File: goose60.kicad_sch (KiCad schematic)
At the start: 1 part

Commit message: add new design
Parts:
- added C1, C2: 22pF, symbol Device:C_Small
- added C3: 1uF, symbol Device:C_Small
- added C4, C5, C6, C7: 100nF, symbol Device:C_Small
- added D1, D2, D3: LED, symbol Device:LED
- added R1, R2: 10K, Resistor_SMD:R_0805_2012Metric, symbol Device:R_Small
- added R3: 300, symbol Device:R_Small
- added SW1, SW2: SW_Push, Button_Switch_SMD:SW_Push_1P1T_NO_CK_KSC6xxJ, symbol Switch:SW_Push
- added X1: Crystal_GND24, symbol Device:Crystal_GND24
- gave numbers to parts that had none: 1
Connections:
- net +3.3V: now reaches U1.1 (VBAT)
- net +3.3V: now also U1.24 (VDD), U1.36 (VDD), U1.48 (VDD), U1.9 (VDDA), C3.1, C4.1, C5.1, C6.1, C7.1, D1.2 (A), D2.2 (A), D3.2 (A), R1.1, R2.1
- net row5: now reaches U1.11 (PA1)
- net row4: now reaches U1.12 (PA2)
- net row3: now reaches U1.13 (PA3)
- net CAPS_LED: now reaches U1.14 (PA4)
- net CAPS_LED: now also R3.2
- net SCK: now reaches U1.15 (PA5)
- net MISO: now reaches U1.16 (PA6)
- net MOSI: now reaches U1.17 (PA7)
- net row2: now reaches U1.18 (PB0)
- net row1: now reaches U1.19 (PB1)
- net col8: now reaches U1.20 (PB2)
- net col9: now reaches U1.21 (PB10)
- net col10: now reaches U1.22 (PB11)
- net GND: now reaches U1.23 (VSS)
- net GND: now also U1.35 (VSS), U1.47 (VSS), U1.8 (VSSA), C1.2, C2.2, C3.2, C4.2, C5.2, C6.2, C7.2, SW1.1, SW2.1, X1.2, X1.4
- net col11: now reaches U1.25 (PB12)
- net col12: now reaches U1.26 (PB13)
- net col13: now reaches U1.27 (PB14)
- net col14: now reaches U1.28 (PB15)
- net MCU_TX: now reaches U1.30 (PA9)
- net MCU_RX: now reaches U1.31 (PA10)
- net USB_D-: now reaches U1.32 (PA11)
- net USB_D+: now reaches U1.33 (PA12)
- net SWDIO: now reaches U1.34 (PA13)
- net SWCLK: now reaches U1.37 (PA14)
- net col1: now reaches U1.39 (PB3)
- net col2: now reaches U1.40 (PB4)
- net col3: now reaches U1.41 (PB5)
- net col4: now reaches U1.42 (PB6)
- net col5: now reaches U1.43 (PB7)
- net BOOT0: now reaches U1.44 (BOOT0)
- net BOOT0: now also R1.2, SW1.2
- net col6: now reaches U1.45 (PB8)
- net col7: now reaches U1.46 (PB9)
- net XTAL1: now reaches U1.5 (PD0)
- net XTAL1: now also C1.1, X1.1
- net XTAL2: now reaches U1.6 (PD1)
- net XTAL2: now also C2.1, X1.3
- net RESET: now reaches U1.7 (NRST)
- net RESET: now also R2.2, SW2.2
- new net: D1.1 (K), D2.1 (K), D3.1 (K), R3.1
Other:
- added sheet Interface (Interface.kicad_sch)
- added sheet PowerManager (PowerManager.kicad_sch)
- added sheet keyswitches (switches.kicad_sch)
- moved on the sheet: U1

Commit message: update goose60 sch footprint
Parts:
- C1, C2, C3, C4, C5, C6, C7: footprint (none) -> Capacitor_SMD:C_0201_0603Metric
- D1, D2, D3: footprint (none) -> LED_SMD:LED_0805_2012Metric
- R3: footprint (none) -> Resistor_SMD:R_0805_2012Metric
- X1: footprint (none) -> Crystal:Crystal_SMD_TXC_7M-4Pin_3.2x2.5mm

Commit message: update components location
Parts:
- C1, C2, C3, C4, C5, C6, C7: footprint Capacitor_SMD:C_0201_0603Metric -> Capacitor_SMD:C_0603_1608Metric
- R1, R2, R3: footprint Resistor_SMD:R_0805_2012Metric -> Resistor_SMD:R_0603_1608Metric
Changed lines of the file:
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@@
       (effects (font (size 1.27 1.27)) (justify left))
     )
-    (property "Footprint" "Capacitor_SMD:C_0201_0603Metric" (id 2) (at 113.03 44.45 0)
+    (property "Footprint" "Capacitor_SMD:C_0603_1608Metric" (id 2) (at 113.03 44.45 0)
       (effects (font (size 1.27 1.27)) hide)
     )
@@
       (effects (font (size 1.27 1.27)) (justify left))
     )
-    (property "Footprint" "Resistor_SMD:R_0805_2012Metric" (id 2) (at 30.48 38.1 0)
+    (property "Footprint" "Resistor_SMD:R_0603_1608Metric" (id 2) (at 30.48 38.1 0)
       (effects (font (size 1.27 1.27)) hide)
     )
@@
       (effects (font (size 1.27 1.27)) (justify left))
     )
-    (property "Footprint" "Capacitor_SMD:C_0201_0603Metric" (id 2) (at 90.17 44.45 0)
+    (property "Footprint" "Capacitor_SMD:C_0603_1608Metric" (id 2) (at 90.17 44.45 0)
       (effects (font (size 1.27 1.27)) hide)
     )
@@
       (effects (font (size 1.27 1.27)) (justify left))
     )
-    (property "Footprint" "Capacitor_SMD:C_0201_0603Metric" (id 2) (at 101.6 44.45 0)
+    (property "Footprint" "Capacitor_SMD:C_0603_1608Metric" (id 2) (at 101.6 44.45 0)
       (effects (font (size 1.27 1.27)) hide)
     )
@@
     (property "Reference" "R3" (id 0) (at 248.92 153.67 90))
     (property "Value" "300" (id 1) (at 248.92 151.13 90))
-    (property "Footprint" "Resistor_SMD:R_0805_2012Metric" (id 2) (at 248.92 148.59 0)
+    (property "Footprint" "Resistor_SMD:R_0603_1608Metric" (id 2) (at 248.92 148.59 0)
       (effects (font (size 1.27 1.27)) hide)
     )
@@
       (effects (font (size 1.27 1.27)) (justify left))
     )
-    (property "Footprint" "Resistor_SMD:R_0805_2012Metric" (id 2) (at 55.88 38.1 0)
+    (property "Footprint" "Resistor_SMD:R_0603_1608Metric" (id 2) (at 55.88 38.1 0)
       (effects (font (size 1.27 1.27)) hide)
     )
@@
       (effects (font (size 1.27 1.27)) (justify left))
     )
-    (property "Footprint" "Capacitor_SMD:C_0201_0603Metric" (id 2) (at 52.07 91.44 0)
+    (property "Footprint" "Capacitor_SMD:C_0603_1608Metric" (id 2) (at 52.07 91.44 0)
       (effects (font (size 1.27 1.27)) hide)
     )
@@
       (effects (font (size 1.27 1.27)) (justify left))
     )
-    (property "Footprint" "Capacitor_SMD:C_0201_0603Metric" (id 2) (at 124.46 44.45 0)
+    (property "Footprint" "Capacitor_SMD:C_0603_1608Metric" (id 2) (at 124.46 44.45 0)
       (effects (font (size 1.27 1.27)) hide)
     )
@@
       (effects (font (size 1.27 1.27)) (justify left))
     )
-    (property "Footprint" "Capacitor_SMD:C_0201_0603Metric" (id 2) (at 80.01 44.45 0)
+    (property "Footprint" "Capacitor_SMD:C_0603_1608Metric" (id 2) (at 80.01 44.45 0)
       (effects (font (size 1.27 1.27)) hide)
     )
@@
       (effects (font (size 1.27 1.27)) (justify left))
     )
-    (property "Footprint" "Capacitor_SMD:C_0201_0603Metric" (id 2) (at 34.29 91.44 0)
+    (property "Footprint" "Capacitor_SMD:C_0603_1608Metric" (id 2) (at 34.29 91.44 0)
       (effects (font (size 1.27 1.27)) hide)
     )
@@
     )
     (path "/f9fe2ed8-a3e3-4d28-b983-2bb5b9d6e010"
-      (reference "C1") (unit 1) (value "22pF") (footprint "Capacitor_SMD:C_0201_0603Metric")
+      (reference "C1") (unit 1) (value "22pF") (footprint "Capacitor_SMD:C_0603_1608Metric")
     )
     (path "/85b1023e-0f04-495c-899c-b4db4874d87f"
-      (reference "C2") (unit 1) (value "22pF") (footprint "Capacitor_SMD:C_0201_0603Metric")
+      (reference "C2") (unit 1) (value "22pF") (footprint "Capacitor_SMD:C_0603_1608Metric")
     )
     (path "/a3141805-9795-46b8-a319-4a53200c12ca"
-      (reference "C3") (unit 1) (value "1uF") (footprint "Capacitor_SMD:C_0201_0603Metric")
+      (reference "C3") (unit 1) (value "1uF") (footprint "Capacitor_SMD:C_0603_1608Metric")
     )
     (path "/5591f67d-166e-4c19-99b1-3b158056aa2d"
-      (reference "C4") (unit 1) (value "100nF") (footprint "Capacitor_SMD:C_0201_0603Metric")
+      (reference "C4") (unit 1) (value "100nF") (footprint "Capacitor_SMD:C_0603_1608Metric")
     )
     (path "/693c6004-a004-4312-bba3-757057e9f797"
-      (reference "C5") (unit 1) (value "100nF") (footprint "Capacitor_SMD:C_0201_0603Metric")
+      (reference "C5") (unit 1) (value "100nF") (footprint "Capacitor_SMD:C_0603_1608Metric")
     )
     (path "/17abe64e-64c1-4764-943d-a43538caeb21"
-      (reference "C6") (unit 1) (value "100nF") (footprint "Capacitor_SMD:C_0201_0603Metric")
+      (reference "C6") (unit 1) (value "100nF") (footprint "Capacitor_SMD:C_0603_1608Metric")
     )
     (path "/88d48de7-d7dd-45f7-8cfd-77da8f4dadfe"
-      (reference "C7") (unit 1) (value "100nF") (footprint "Capacitor_SMD:C_0201_0603Metric")
+      (reference "C7") (unit 1) (value "100nF") (footprint "Capacitor_SMD:C_0603_1608Metric")
     )
     (path "/01ad3d1c-4e51-419d-9147-129ed3c97a58/59366270-d046-4a8d-8a86-fa3f9d2a71fc"
-      (reference "C8") (unit 1) (value "100nF/16v") (footprint "Capacitor_SMD:C_0201_0603Metric")
+      (reference "C8") (unit 1) (value "100nF/16v") (footprint "Capacitor_SMD:C_0603_1608Metric")
     )
     (path "/01ad3d1c-4e51-419d-9147-129ed3c97a58/f33d1f7b-69f3-44d0-8d3e-63e68406121a"
-      (reference "C9") (unit 1) (value "10uF/16v") (footprint "Capacitor_SMD:C_0201_0603Metric")
+      (reference "C9") (unit 1) (value "10uF/16v") (footprint "Capacitor_SMD:C_0603_1608Metric")
     )
     (path "/01ad3d1c-4e51-419d-9147-129ed3c97a58/c9bdc69b-046c-48e6-81b1-bae8188675f3"
-      (reference "C10") (unit 1) (value "100uF/16v") (footprint "Capacitor_SMD:C_0201_0603Metric")
+      (reference "C10") (unit 1) (value "100uF/16v") (footprint "Capacitor_SMD:C_0603_1608Metric")
     )
     (path "/01ad3d1c-4e51-419d-9147-129ed3c97a58/6bfc3026-825b-4595-81dc-f862b2691dba"
-      (reference "C11") (unit 1) (value "100nF/16v") (footprint "Capacitor_SMD:C_0201_0603Metric")
+      (reference "C11") (unit 1) (value "100nF/16v") (footprint "Capacitor_SMD:C_0603_1608Metric")
     )
     (path "/a91e1d94-3d93-4a93-b820-1f6e8519d9a9"
@@
     )
     (path "/01ad3d1c-4e51-419d-9147-129ed3c97a58/5ebc741d-6cfd-4dfe-84d0-b07ee0e888cf"
-      (reference "D69") (unit 1) (value "6.3V/100V") (footprint "Diode_SMD:D_SOD-323F")
+      (reference "D69") (unit 1) (value "6.3V/100V") (footprint "Diode_SMD:D_0603_1608Metric")
     )
     (path "/01ad3d1c-4e51-419d-9147-129ed3c97a58/e45f4eff-fcf1-42db-a4e4-d19097900666"
-      (reference "D70") (unit 1) (value "1SS355TE") (footprint "Diode_SMD:D_SOD-323F")
+      (reference "D70") (unit 1) (value "1SS355TE") (footprint "Diode_SMD:D_0603_1608Metric")
     )
     (path "/62b6fb8f-6304-48f3-b35d-3d0f8813eb4a/693deba9-5b7b-47eb-a076-785918ecb9b5"
@@
     )
     (path "/24d5275e-ddc5-47af-b388-ecc08567cc69"
-      (reference "R1") (unit 1) (value "10K") (footprint "Resistor_SMD:R_0805_2012Metric")
+      (reference "R1") (unit 1) (value "10K") (footprint "Resistor_SMD:R_0603_1608Metric")
     )
     (path "/80049181-0e53-46a8-92f2-82ffb9ac51b9"
-      (reference "R2") (unit 1) (value "10K") (footprint "Resistor_SMD:R_0805_2012Metric")
+      (reference "R2") (unit 1) (value "10K") (footprint "Resistor_SMD:R_0603_1608Metric")
     )
     (path "/6a760a19-5869-4605-bfdf-467b2efd2302"
-      (reference "R3") (unit 1) (value "300") (footprint "Resistor_SMD:R_0805_2012Metric")
+      (reference "R3") (unit 1) (value "300") (footprint "Resistor_SMD:R_0603_1608Metric")
     )
     (path "/01ad3d1c-4e51-419d-9147-129ed3c97a58/58c52a8a-44f3-4097-86b6-0bb03693e54a"
-      (reference "R4") (unit 1) (value "240R/5%") (footprint "Resistor_SMD:R_0805_2012Metric")
+      (reference "R4") (unit 1) (value "240R/5%") (footprint "Resistor_SMD:R_0603_1608Metric")
     )
     (path "/01ad3d1c-4e51-419d-9147-129ed3c97a58/ffd8a55c-ebe3-49d3-8e38-b48450d53cd0"
-      (reference "R5") (unit 1) (value "820R/5%") (footprint "Resistor_SMD:R_0805_2012Metric")
+      (reference "R5") (unit 1) (value "820R/5%") (footprint "Resistor_SMD:R_0603_1608Metric")
     )
     (path "/01ad3d1c-4e51-419d-9147-129ed3c97a58/8fc35c16-fc9a-4e74-93e4-98f97ca6399b"
-      (reference "R6") (unit 1) (value "820R/5%") (footprint "Resistor_SMD:R_0805_2012Metric")
+      (reference "R6") (unit 1) (value "820R/5%") (footprint "Resistor_SMD:R_0603_1608Metric")
     )
     (path "/62b6fb8f-6304-48f3-b35d-3d0f8813eb4a/916bb521-d79a-4258-8831-772571d1f9b5"
-      (reference "R7") (unit 1) (value "10K") (footprint "Resistor_SMD:R_0805_2012Metric")
+      (reference "R7") (unit 1) (value "10K") (footprint "Resistor_SMD:R_0603_1608Metric")
     )
     (path "/62b6fb8f-6304-48f3-b35d-3d0f8813eb4a/052e406a-cd5c-4294-8787-61de419cd69b"
-      (reference "R8") (unit 1) (value "10K") (footprint "Resistor_SMD:R_0805_2012Metric")
+      (reference "R8") (unit 1) (value "10K") (footprint "Resistor_SMD:R_0603_1608Metric")
     )
     (path "/62b6fb8f-6304-48f3-b35d-3d0f8813eb4a/baffa815-068c-492b-b76f-cfe58c1daf53"
@@
     )
     (path "/62b6fb8f-6304-48f3-b35d-3d0f8813eb4a/75fd90a4-2c53-46a9-93a4-07f79f00b17a"
-      (reference "R12") (unit 1) (value "0") (footprint "Resistor_SMD:R_0805_2012Metric")
+      (reference "R12") (unit 1) (value "0") (footprint "Resistor_SMD:R_0603_1608Metric")
     )
     (path "/62b6fb8f-6304-48f3-b35d-3d0f8813eb4a/bbf19c51-7502-4c71-bd92-745e7b08f5a5"
-      (reference "R13") (unit 1) (value "0") (footprint "Resistor_SMD:R_0805_2012Metric")
+      (reference "R13") (unit 1) (value "0") (footprint "Resistor_SMD:R_0603_1608Metric")
     )
     (path "/62b6fb8f-6304-48f3-b35d-3d0f8813eb4a/3a4d123e-3d6c-458b-8cdb-27ddea7e40e5"
-      (reference "R14") (unit 1) (value "0") (footprint "Resistor_SMD:R_0805_2012Metric")
+      (reference "R14") (unit 1) (value "0") (footprint "Resistor_SMD:R_0603_1608Metric")
     )
     (path "/4b620212-7d38-40bd-8ffb-1e64542d8c37"

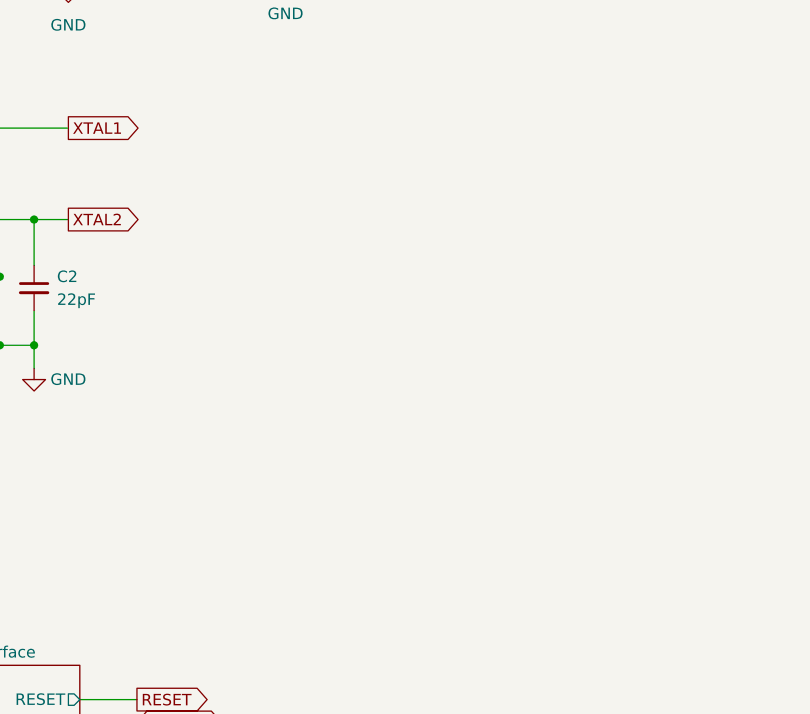
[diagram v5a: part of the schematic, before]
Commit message: update MX socket loaction
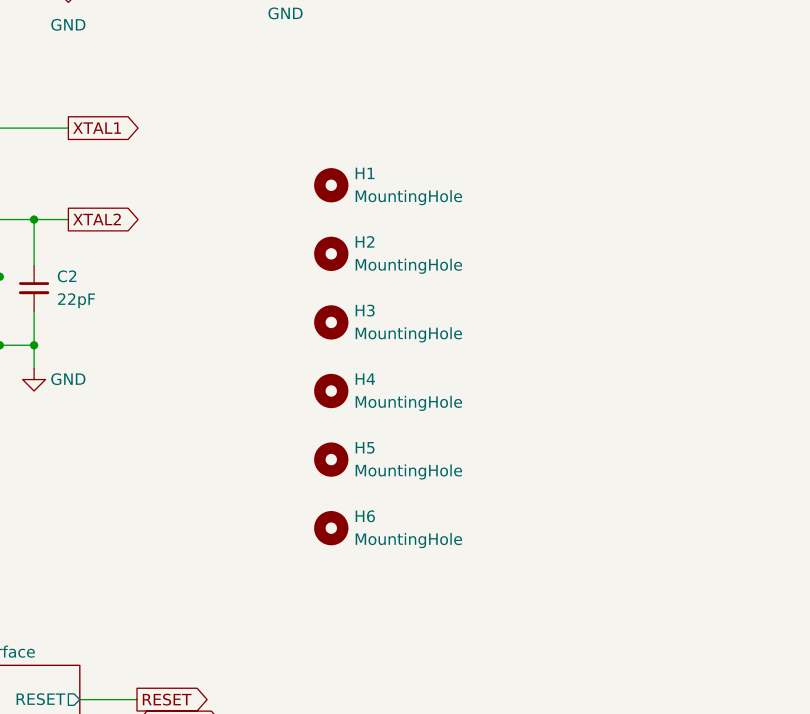
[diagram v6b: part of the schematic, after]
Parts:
- added H1, H2, H3, H5, H6: MountingHole, MountingHole:MountingHole_3.2mm_M3_Pad, symbol Mechanical:MountingHole
- added H4: MountingHole, MountingHole:MountingHole_3.2mm_M3, symbol Mechanical:MountingHole
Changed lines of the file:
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@@
     (pin "2")
+  )
+  (symbol (lib_id "Mechanical:MountingHole") (at 85.09 95.25 0) (unit 1)
+    (in_bom yes) (on_board yes) (fields_autoplaced)
+    (property "Reference" "H3" (id 0) (at 87.63 93.9799 0)
+      (effects (font (size 1.27 1.27)) (justify left))
+    )
+    (property "Value" "MountingHole" (id 1) (at 87.63 96.5199 0)
+      (effects (font (size 1.27 1.27)) (justify left))
+    )
+    (property "Footprint" "MountingHole:MountingHole_3.2mm_M3_Pad" (id 2) (at 85.09 95.25 0)
+      (effects (font (size 1.27 1.27)) hide)
+    )
+    (property "Datasheet" "~" (id 3) (at 85.09 95.25 0)
+      (effects (font (size 1.27 1.27)) hide)
+    )
   )
   (symbol (lib_id "power:+3.3V") (at 257.81 123.19 0) (unit 1)
@@
     (pin "1")
     (pin "2")
+  )
+  (symbol (lib_id "Mechanical:MountingHole") (at 85.09 102.87 0) (unit 1)
+    (in_bom yes) (on_board yes) (fields_autoplaced)
+    (property "Reference" "H4" (id 0) (at 87.63 101.5999 0)
+      (effects (font (size 1.27 1.27)) (justify left))
+    )
+    (property "Value" "MountingHole" (id 1) (at 87.63 104.1399 0)
+      (effects (font (size 1.27 1.27)) (justify left))
+    )
+    (property "Footprint" "MountingHole:MountingHole_3.2mm_M3" (id 2) (at 85.09 102.87 0)
+      (effects (font (size 1.27 1.27)) hide)
+    )
+    (property "Datasheet" "~" (id 3) (at 85.09 102.87 0)
+      (effects (font (size 1.27 1.27)) hide)
+    )
   )
   (symbol (lib_id "Device:C_Small") (at 101.6 44.45 0) (unit 1)
@@
     (pin "1")
     (pin "2")
+  )
+  (symbol (lib_id "Mechanical:MountingHole") (at 85.09 87.63 0) (unit 1)
+    (in_bom yes) (on_board yes) (fields_autoplaced)
+    (property "Reference" "H2" (id 0) (at 87.63 86.3599 0)
+      (effects (font (size 1.27 1.27)) (justify left))
+    )
+    (property "Value" "MountingHole" (id 1) (at 87.63 88.8999 0)
+      (effects (font (size 1.27 1.27)) (justify left))
+    )
+    (property "Footprint" "MountingHole:MountingHole_3.2mm_M3_Pad" (id 2) (at 85.09 87.63 0)
+      (effects (font (size 1.27 1.27)) hide)
+    )
+    (property "Datasheet" "~" (id 3) (at 85.09 87.63 0)
+      (effects (font (size 1.27 1.27)) hide)
+    )
+  )
+  (symbol (lib_id "Mechanical:MountingHole") (at 85.09 110.49 0) (unit 1)
+    (in_bom yes) (on_board yes) (fields_autoplaced)
+    (property "Reference" "H5" (id 0) (at 87.63 109.2199 0)
+      (effects (font (size 1.27 1.27)) (justify left))
+    )
+    (property "Value" "MountingHole" (id 1) (at 87.63 111.7599 0)
+      (effects (font (size 1.27 1.27)) (justify left))
+    )
+    (property "Footprint" "MountingHole:MountingHole_3.2mm_M3_Pad" (id 2) (at 85.09 110.49 0)
+      (effects (font (size 1.27 1.27)) hide)
+    )
+    (property "Datasheet" "~" (id 3) (at 85.09 110.49 0)
+      (effects (font (size 1.27 1.27)) hide)
+    )
   )
   (symbol (lib_id "Device:LED") (at 257.81 135.89 90) (unit 1)
@@
     (pin "9")
   )
+  (symbol (lib_id "Mechanical:MountingHole") (at 85.09 80.01 0) (unit 1)
+    (in_bom yes) (on_board yes) (fields_autoplaced)
+    (property "Reference" "H1" (id 0) (at 87.63 78.7399 0)
+      (effects (font (size 1.27 1.27)) (justify left))
+    )
+    (property "Value" "MountingHole" (id 1) (at 87.63 81.2799 0)
+      (effects (font (size 1.27 1.27)) (justify left))
+    )
+    (property "Footprint" "MountingHole:MountingHole_3.2mm_M3_Pad" (id 2) (at 85.09 80.01 0)
+      (effects (font (size 1.27 1.27)) hide)
+    )
+    (property "Datasheet" "~" (id 3) (at 85.09 80.01 0)
+      (effects (font (size 1.27 1.27)) hide)
+    )
+  )
+  (symbol (lib_id "Mechanical:MountingHole") (at 85.09 118.11 0) (unit 1)
+    (in_bom yes) (on_board yes) (fields_autoplaced)
+    (property "Reference" "H6" (id 0) (at 87.63 116.8399 0)
+      (effects (font (size 1.27 1.27)) (justify left))
+    )
+    (property "Value" "MountingHole" (id 1) (at 87.63 119.3799 0)
+      (effects (font (size 1.27 1.27)) (justify left))
+    )
+    (property "Footprint" "MountingHole:MountingHole_3.2mm_M3_Pad" (id 2) (at 85.09 118.11 0)
+      (effects (font (size 1.27 1.27)) hide)
+    )
+    (property "Datasheet" "~" (id 3) (at 85.09 118.11 0)
+      (effects (font (size 1.27 1.27)) hide)
+    )
+  )
   (symbol (lib_id "power:GND") (at 38.1 170.18 0) (unit 1)
     (in_bom yes) (on_board yes) (fields_autoplaced)
@@
       (reference "D70") (unit 1) (value "1SS355TE") (footprint "Diode_SMD:D_0603_1608Metric")
     )
+    (path "/e5255316-baa4-4e6b-b2de-4b7fd45b19cb"
+      (reference "H1") (unit 1) (value "MountingHole") (footprint "MountingHole:MountingHole_3.2mm_M3_Pad")
+    )
+    (path "/b34b0885-1966-40a8-9043-234e7293b68d"
+      (reference "H2") (unit 1) (value "MountingHole") (footprint "MountingHole:MountingHole_3.2mm_M3_Pad")
+    )
+    (path "/194c0306-fe3c-424b-a3f0-c7703c93c3ff"
+      (reference "H3") (unit 1) (value "MountingHole") (footprint "MountingHole:MountingHole_3.2mm_M3_Pad")
+    )
+    (path "/68003b77-68f6-438d-ae58-7257fdc6e943"
+      (reference "H4") (unit 1) (value "MountingHole") (footprint "MountingHole:MountingHole_3.2mm_M3")
+    )
+    (path "/d67504c4-2a08-4885-9174-43c4aa4a0de7"
+      (reference "H5") (unit 1) (value "MountingHole") (footprint "MountingHole:MountingHole_3.2mm_M3_Pad")
+    )
+    (path "/e633e322-95ba-4703-893c-9de214c02b51"
+      (reference "H6") (unit 1) (value "MountingHole") (footprint "MountingHole:MountingHole_3.2mm_M3_Pad")
+    )
     (path "/62b6fb8f-6304-48f3-b35d-3d0f8813eb4a/693deba9-5b7b-47eb-a076-785918ecb9b5"
